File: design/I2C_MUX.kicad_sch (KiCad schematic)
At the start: 26 parts

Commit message: new power converter added
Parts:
- C40: renamed from C?; value (none) -> CC0201_100NF_6.3V_10%_X5R; footprint (none) -> CAPC0603X33N
- J20: value (none) -> Test connector; footprint (none) -> Connector_PinHeader_2.54mm:PinHeader_1x14_P2.54mm_Vertical
- R274, R42, R43, R44: renamed from R?; value (none) -> R0402_0R_JUMPER; footprint (none) -> RESC1005X40N
- R39, R40, R41, R45, R46, R47, R48, R49, R50, R51, R52, R53, R54, R55, R56, R57, R75, R83, R91: value (none) -> R0402_2K2_1%_0.0625W_100PPM; footprint (none) -> RESC1005X40N
- U5: value (none) -> TCA9548ARGER; footprint (none) -> ICs And Semiconductors SMD:QFN50P400X400X100-25N-S220

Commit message: connected signals to the J9 connector
connected signals to the J9 connector
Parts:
- C40, R274, R39, R40, R41, R42, R43, R44, R45, R46, R47, R48, R49, R50, R51, R52, R53, R54, R55, R56, R57, R75, R83, R91: Author CERN DEM JLC -> (none)
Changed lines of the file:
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@@
       (effects (font (size 1.524 1.524)) (justify left) hide)
     )
-    (property "Author" "CERN DEM JLC" (id 36) (at 116.84 -6.35 0)
+    (property "Author" "" (id 36) (at 116.84 -6.35 0)
       (effects (font (size 1.524 1.524)) (justify left) hide)
     )
@@
       (effects (font (size 1.524 1.524)) (justify left) hide)
     )
-    (property "Author" "CERN DEM JLC" (id 36) (at 116.84 -3.81 0)
+    (property "Author" "" (id 36) (at 116.84 -3.81 0)
       (effects (font (size 1.524 1.524)) (justify left) hide)
     )
@@
       (effects (font (size 1.524 1.524)) (justify left) hide)
     )
-    (property "Author" "CERN DEM JLC" (id 36) (at 116.84 -1.27 0)
+    (property "Author" "" (id 36) (at 116.84 -1.27 0)
       (effects (font (size 1.524 1.524)) (justify left) hide)
     )
@@
       (effects (font (size 1.524 1.524)) (justify left) hide)
     )
-    (property "Author" "CERN DEM JLC" (id 36) (at 165.1 142.24 0)
+    (property "Author" "" (id 36) (at 165.1 142.24 0)
       (effects (font (size 1.524 1.524)) (justify left) hide)
     )
@@
       (effects (font (size 1.524 1.524)) (justify left) hide)
     )
-    (property "Author" "CERN DEM JLC" (id 36) (at 165.1 144.78 0)
+    (property "Author" "" (id 36) (at 165.1 144.78 0)
       (effects (font (size 1.524 1.524)) (justify left) hide)
     )
@@
       (effects (font (size 1.524 1.524)) (justify left) hide)
     )
-    (property "Author" "CERN DEM JLC" (id 36) (at 165.1 147.32 0)
+    (property "Author" "" (id 36) (at 165.1 147.32 0)
       (effects (font (size 1.524 1.524)) (justify left) hide)
     )
@@
       (effects (font (size 1.524 1.524)) (justify left) hide)
     )
-    (property "Author" "CERN DEM JLC" (id 36) (at 165.1 149.86 0)
+    (property "Author" "" (id 36) (at 165.1 149.86 0)
       (effects (font (size 1.524 1.524)) (justify left) hide)
     )
@@
       (effects (font (size 1.524 1.524)) (justify left) hide)
     )
-    (property "Author" "CERN DEM JLC" (id 36) (at 152.4 152.4 0)
+    (property "Author" "" (id 36) (at 152.4 152.4 0)
       (effects (font (size 1.524 1.524)) (justify left) hide)
     )
@@
       (effects (font (size 1.524 1.524)) (justify left) hide)
     )
-    (property "Author" "CERN DEM JLC" (id 36) (at 152.4 154.94 0)
+    (property "Author" "" (id 36) (at 152.4 154.94 0)
       (effects (font (size 1.524 1.524)) (justify left) hide)
     )
@@
       (effects (font (size 1.524 1.524)) (justify left) hide)
     )
-    (property "Author" "CERN DEM JLC" (id 36) (at 165.1 157.48 0)
+    (property "Author" "" (id 36) (at 165.1 157.48 0)
       (effects (font (size 1.524 1.524)) (justify left) hide)
     )
@@
       (effects (font (size 1.524 1.524)) (justify left) hide)
     )
-    (property "Author" "CERN DEM JLC" (id 36) (at 165.1 160.02 0)
+    (property "Author" "" (id 36) (at 165.1 160.02 0)
       (effects (font (size 1.524 1.524)) (justify left) hide)
     )
@@
       (effects (font (size 1.524 1.524)) (justify left) hide)
     )
-    (property "Author" "CERN DEM JLC" (id 36) (at 152.4 162.56 0)
+    (property "Author" "" (id 36) (at 152.4 162.56 0)
       (effects (font (size 1.524 1.524)) (justify left) hide)
     )
@@
       (effects (font (size 1.524 1.524)) (justify left) hide)
     )
-    (property "Author" "CERN DEM JLC" (id 36) (at 152.4 165.1 0)
+    (property "Author" "" (id 36) (at 152.4 165.1 0)
       (effects (font (size 1.524 1.524)) (justify left) hide)
     )
@@
       (effects (font (size 1.524 1.524)) (justify left) hide)
     )
-    (property "Author" "CERN DEM JLC" (id 36) (at 152.4 167.64 0)
+    (property "Author" "" (id 36) (at 152.4 167.64 0)
       (effects (font (size 1.524 1.524)) (justify left) hide)
     )
@@
       (effects (font (size 1.524 1.524)) (justify left) hide)
     )
-    (property "Author" "CERN DEM JLC" (id 36) (at 152.4 170.18 0)
+    (property "Author" "" (id 36) (at 152.4 170.18 0)
       (effects (font (size 1.524 1.524)) (justify left) hide)
     )
@@
       (effects (font (size 1.524 1.524)) (justify left) hide)
     )
-    (property "Author" "CERN DEM JLC" (id 36) (at 165.1 172.72 0)
+    (property "Author" "" (id 36) (at 165.1 172.72 0)
       (effects (font (size 1.524 1.524)) (justify left) hide)
     )
@@
       (effects (font (size 1.524 1.524)) (justify left) hide)
     )
-    (property "Author" "CERN DEM JLC" (id 36) (at 165.1 175.26 0)
+    (property "Author" "" (id 36) (at 165.1 175.26 0)
       (effects (font (size 1.524 1.524)) (justify left) hide)
     )
@@
       (effects (font (size 1.524 1.524)) (justify left) hide)
     )
-    (property "Author" "CERN DEM JLC" (id 36) (at 152.4 177.8 0)
+    (property "Author" "" (id 36) (at 152.4 177.8 0)
       (effects (font (size 1.524 1.524)) (justify left) hide)
     )
@@
       (effects (font (size 1.524 1.524)) (justify left) hide)
     )
-    (property "Author" "CERN DEM JLC" (id 36) (at 152.4 180.34 0)
+    (property "Author" "" (id 36) (at 152.4 180.34 0)
       (effects (font (size 1.524 1.524)) (justify left) hide)
     )
@@
       (effects (font (size 1.524 1.524)) (justify left) hide)
     )
-    (property "Author" "CERN DEM JLC" (id 36) (at 15.24 44.45 0)
+    (property "Author" "" (id 36) (at 15.24 44.45 0)
       (effects (font (size 1.524 1.524)) (justify left) hide)
     )
@@
       (effects (font (size 1.524 1.524)) (justify left) hide)
     )
-    (property "Author" "CERN DEM JLC" (id 36) (at 20.32 44.45 0)
+    (property "Author" "" (id 36) (at 20.32 44.45 0)
       (effects (font (size 1.524 1.524)) (justify left) hide)
     )
@@
       (effects (font (size 1.524 1.524)) (justify left) hide)
     )
-    (property "Author" "CERN DEM JLC" (id 36) (at 25.4 44.45 0)
+    (property "Author" "" (id 36) (at 25.4 44.45 0)
       (effects (font (size 1.524 1.524)) (justify left) hide)
     )
@@
       (effects (font (size 1.524 1.524)) (justify left) hide)
     )
-    (property "Author" "CERN DEM JLC" (id 35) (at 120.65 132.334 0)
+    (property "Author" "" (id 35) (at 120.65 132.334 0)
       (effects (font (size 1.524 1.524)) (justify left) hide)
     )
@@
       (effects (font (size 1.524 1.524)) (justify left) hide)
     )
-    (property "Author" "CERN DEM JLC" (id 36) (at 30.48 72.39 0)
-      (effects (font (size 1.524 1.524)) (justify left) hide)
-    )
+    (property "Author" "" (id 36) (at 30.48 72.39 0)
+      (effects (font (size 1.524 1.524)) (justify left) hide)
+    )

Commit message: Attempt to add and improve BOM. Added new part numbers for some of the passives
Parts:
- R274, R42, R43, R44: MANUFACTURER (none) -> GENERIC
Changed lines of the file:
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@@
       (effects (font (size 1.524 1.524)) (justify left) hide)
+    )
+    (property "MANUFACTURER" "GENERIC" (id 41) (at 116.84 81.28 0)
+      (effects (font (size 1.27 1.27)) hide)
     )
     (pin "1")
@@
       (effects (font (size 1.524 1.524)) (justify left) hide)
     )
+    (property "MANUFACTURER" "GENERIC" (id 41) (at 116.84 83.82 0)
+      (effects (font (size 1.27 1.27)) hide)
+    )
     (pin "1")
     (pin "2")
@@
     (property "License" "This work is licensed under the Creative Commons CC-BY-SA 4.0 License. To the extent that circuit schematics that use Licensed Material can be considered to be ‘Adapted Material’, then the copyright holder waives article 3.b of the license with respect to these schematics." (id 40) (at 116.84 -10.414 0)
       (effects (font (size 1.524 1.524)) (justify left) hide)
+    )
+    (property "MANUFACTURER" "GENERIC" (id 41) (at 116.84 86.36 0)
+      (effects (font (size 1.27 1.27)) hide)
     )
     (pin "1")
@@
       (effects (font (size 1.27 1.27)) hide)
     )
+    (property "MANUFACTURER" "GENERIC" (id 42) (at 118.11 72.39 0)
+      (effects (font (size 1.27 1.27)) hide)
+    )

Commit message: Restore some consistency in schematic metadata
Still 13 problematic footprint names in LTM4673.kicad_sch:

BAD Dup: "Footprint" "CAPC1608X87N" "Capacitors SMD:CAPC1005X55N" in LTM4673-altium-import:0_Capacitor - non polarized
BAD Dup: "Footprint" "CAPC2012X135N" "CAPC1608X87N" in LTM4673-altium-import:1_Capacitor - non polarized
BAD Dup: "Footprint" "CAPC1608X87N" "Capacitors SMD:CAPC1005X55N" in LTM4673-altium-import:1_Capacitor - non polarized
BAD Dup: "Footprint" "CAPC3216X180N" "CAPC3225X270N" in LTM4673-altium-import:1_Capacitor - non polarized
BAD Dup: "Footprint" "CAPC1608X87N" "Capacitors SMD:CAPC1005X55N" in LTM4673-altium-import:0_Capacitor - non polarized
BAD Dup: "Footprint" "CAPC1608X87N" "Capacitors SMD:CAPC1005X55N" in LTM4673-altium-import:0_Capacitor - non polarized
BAD Dup: "Footprint" "CAPC3216X180N" "CAPC3225X270N" in LTM4673-altium-import:1_Capacitor - non polarized
BAD Dup: "Footprint" "CAPC2012X135N" "CAPC1608X87N" in LTM4673-altium-import:1_Capacitor - non polarized
BAD Dup: "Footprint" "CAPC3216X180N" "CAPC3225X270N" in LTM4673-altium-import:1_Capacitor - non polarized
BAD Dup: "Footprint" "CAPC1608X87N" "Capacitors SMD:CAPC1005X55N" in LTM4673-altium-import:0_Capacitor - non polarized
BAD Dup: "Footprint" "CAPC1608X87N" "Capacitors SMD:CAPC1005X55N" in LTM4673-altium-import:1_Capacitor - non polarized
BAD Dup: "Footprint" "CAPC3216X180N" "CAPC3225X270N" in LTM4673-altium-import:1_Capacitor - non polarized
BAD Dup: "Footprint" "CAPMP7343X310N" "Capacitor_Tantalum_SMD:CP_EIA-7343-30_AVX-N" in LTM4673-altium-import:3_Capacitor - polarized

But the Symbol Field editor in eeschema should be more useful now.
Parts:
- R274, R42, R43, R44: MANUFACTURER GENERIC -> (none)
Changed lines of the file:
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@@
       (effects (font (size 1.524 1.524)) (justify left) hide)
-    )
-    (property "MANUFACTURER" "GENERIC" (id 41) (at 116.84 81.28 0)
-      (effects (font (size 1.27 1.27)) hide)
     )
     (pin "1")
@@
       (effects (font (size 1.524 1.524)) (justify left) hide)
     )
-    (property "MANUFACTURER" "GENERIC" (id 41) (at 116.84 83.82 0)
-      (effects (font (size 1.27 1.27)) hide)
-    )
     (pin "1")
     (pin "2")
@@
     (property "License" "This work is licensed under the Creative Commons CC-BY-SA 4.0 License. To the extent that circuit schematics that use Licensed Material can be considered to be ‘Adapted Material’, then the copyright holder waives article 3.b of the license with respect to these schematics." (id 40) (at 116.84 -10.414 0)
       (effects (font (size 1.524 1.524)) (justify left) hide)
-    )
-    (property "MANUFACTURER" "GENERIC" (id 41) (at 116.84 86.36 0)
-      (effects (font (size 1.27 1.27)) hide)
     )
     (pin "1")
@@
       (effects (font (size 1.27 1.27)) hide)
     )
-    (property "MANUFACTURER" "GENERIC" (id 42) (at 118.11 72.39 0)
-      (effects (font (size 1.27 1.27)) hide)
-    )

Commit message: Remove unused J21; mark J20 and J22 as dnf
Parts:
- J20: config (none) -> dnf
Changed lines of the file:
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@@
+      (effects (font (size 1.27 1.27)) hide)
+    )
+    (property "config" "dnf" (id 4) (at 186.69 123.19 0)
       (effects (font (size 1.27 1.27)) hide)
     )

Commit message: Convert MMC version from v1.3 to v1.4, and fuss with DNP/dnf attributes
Hope result is more accurate and less confusing
Change R274 to 2k2 with visible config=dnf attribute
Change R147 to 1k with visible config=dnf attribute
Change R158 to remove config=dnf attribute
Adjust text documenting MMC versions to say DNF instead of DNP
Add visible config=dnf attribute
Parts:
- R274: ~ DNP -> 2k2
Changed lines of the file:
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@@
       (effects (font (size 1.524 1.524)) (justify left) hide)
     )
-    (property "~" "DNP" (id 4) (at 120.65 76.2 0))
+    (property "~" "2k2" (id 4) (at 120.65 76.2 0))
     (property "Part Number" "R0402_0R_JUMPER" (id 5) (at 105.918 72.39 0)
       (effects (font (size 1.524 1.524)) (justify left) hide)
@@
       (effects (font (size 1.524 1.524)) (justify left) hide)
     )
-    (property "config" "dnf" (id 41) (at 118.11 72.39 0)
-      (effects (font (size 1.27 1.27)) hide)
-    )
+    (property "config" "dnf" (id 41) (at 121.92 76.2 0))
     (pin "1")
     (pin "2")

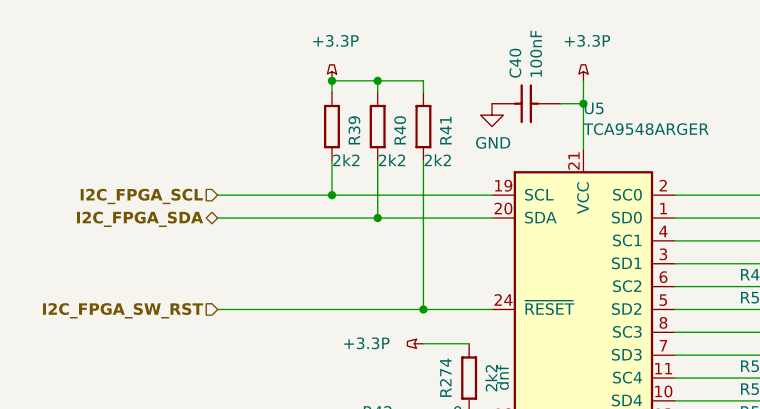
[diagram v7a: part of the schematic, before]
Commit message: R39, R40 -> 4k99
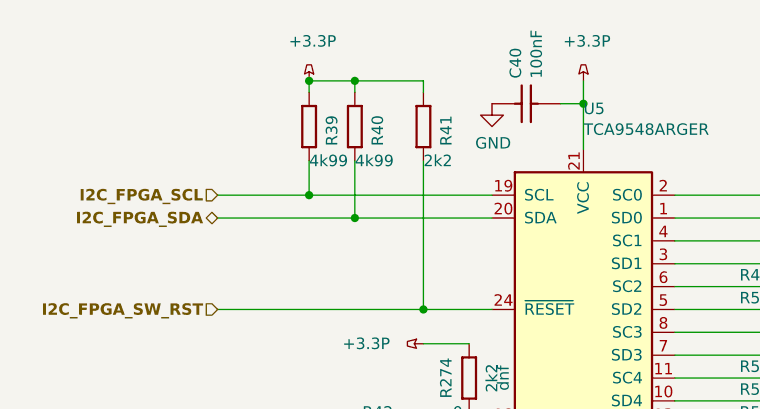
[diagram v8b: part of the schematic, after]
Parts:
- R39, R40: value R0402_2K2_1%_0.0625W_100PPM -> R0402_4k99_1%_0.0625W_100PPM; Manufacturer Part Number R0402_2K2_1%_0.0625W_100PPM -> R0402_4k99_1%_0.0625W_100PPM; Manufacturer1 Part Number 232270672202L -> (none); Part Number R0402_2K2_1%_0.0625W_100PPM -> R0402_4k99_1%_0.0625W_100PPM; Val 2k2 -> 4k99; ~ 2k2 -> 4k99
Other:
- moved on the sheet: R39, R40
